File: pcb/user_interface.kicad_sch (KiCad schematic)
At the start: 18 parts, among them Q6 NTR4003N, SW4 GSPTS0018, SW5 GSPTS0018, SW6 GSPTS0018, SW7 GSPTS0018

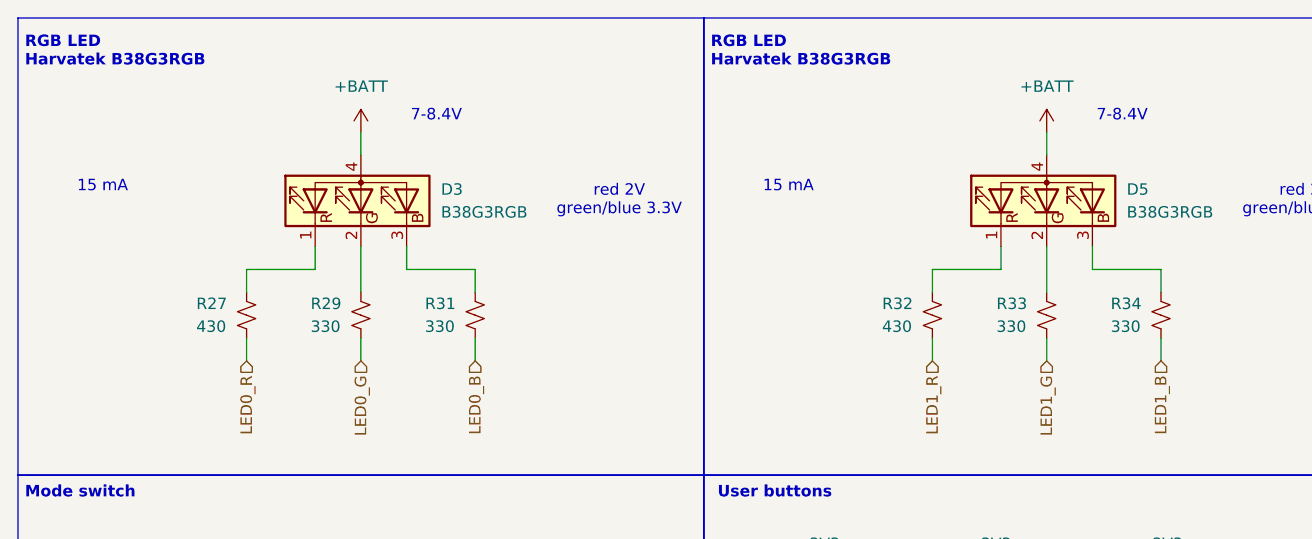
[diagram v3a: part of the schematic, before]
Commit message: Decrease LED current from 15 mA to 10 mA per color
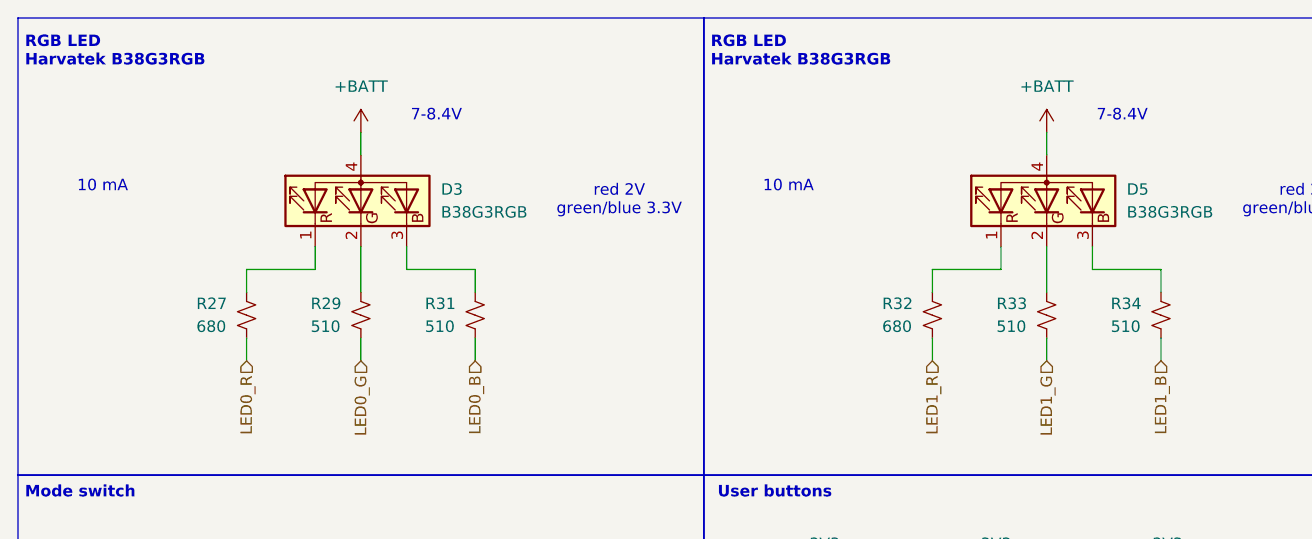
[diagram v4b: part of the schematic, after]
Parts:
- R27, R32: value 430 -> 680
- R29, R31, R33, R34: value 330 -> 510
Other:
- note added: "10 mA"
- note removed: "15 mA"
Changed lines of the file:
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@@
 		)
 	)
-	(text "15 mA"
+	(text "10 mA"
 		(exclude_from_sim no)
 		(at 22.098 31.496 0)
@@
 		)
 	)
-	(text "15 mA"
+	(text "10 mA"
 		(exclude_from_sim no)
 		(at 98.298 31.496 0)
@@
 			)
 		)
-		(property "Value" "330"
+		(property "Value" "510"
 			(at 45.212 46.99 0)
 			(effects
@@
 			)
 		)
-		(property "Value" "330"
+		(property "Value" "510"
 			(at 121.412 46.99 0)
 			(effects
@@
 			)
 		)
-		(property "Value" "430"
+		(property "Value" "680"
 			(at 108.712 46.99 0)
 			(effects
@@
 			)
 		)
-		(property "Value" "330"
+		(property "Value" "510"
 			(at 134.112 46.99 0)
 			(effects
@@
 			)
 		)
-		(property "Value" "430"
+		(property "Value" "680"
 			(at 32.512 46.99 0)
 			(effects
@@
 			)
 		)
-		(property "Value" "330"
+		(property "Value" "510"
 			(at 57.912 46.99 0)
 			(effects

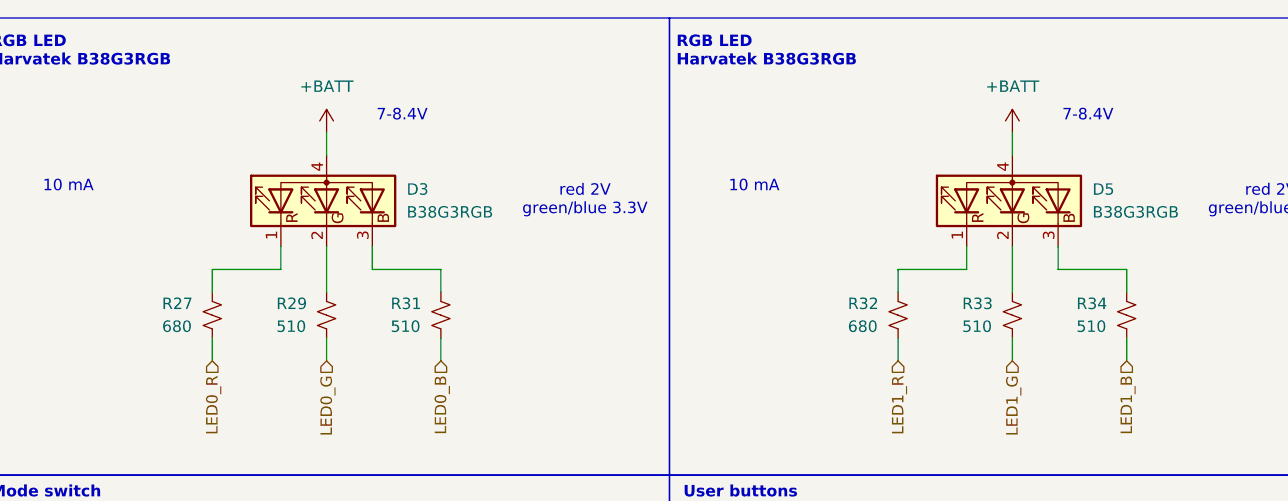
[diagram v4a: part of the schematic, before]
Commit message: Finish routing with rotated STM32
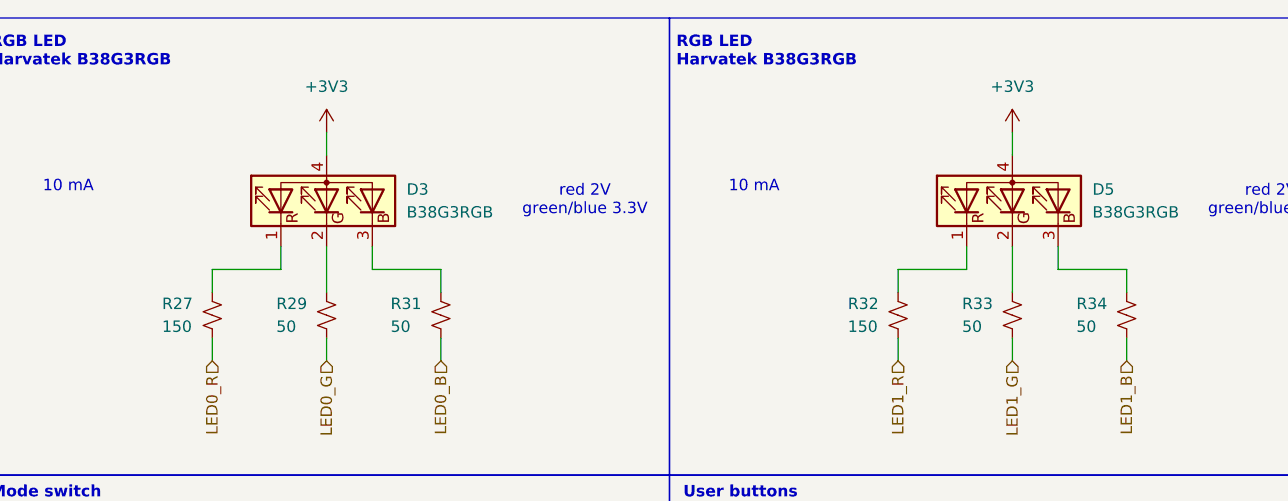
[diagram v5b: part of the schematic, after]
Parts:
- R27, R32: value 680 -> 150
- R29, R31, R33, R34: value 510 -> 50
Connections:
- net +BATT is gone; now on net +3V3: D3.4 (A), D5.4 (A)
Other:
- note removed: "7-8.4V"
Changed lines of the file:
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@@
-		)
-	)
-	(text "7-8.4V"
-		(exclude_from_sim no)
-		(at 59.182 23.622 0)
-		(effects
-			(font
-				(size 1.27 1.27)
-			)
-		)
-	)
-	(text "7-8.4V"
-		(exclude_from_sim no)
-		(at 135.382 23.622 0)
-		(effects
-			(font
-				(size 1.27 1.27)
-			)
 		)
 	)
@@
 			)
 		)
-		(property "Value" "510"
+		(property "Value" "50"
 			(at 45.212 46.99 0)
 			(effects
@@
 	(symbol
 		(lib_id "power:+3V3")
+		(at 127 25.4 0)
+		(unit 1)
+		(exclude_from_sim no)
+		(in_bom yes)
+		(on_board yes)
+		(dnp no)
+		(fields_autoplaced yes)
+		(property "Reference" "#PWR065"
+			(at 127 29.21 0)
+			(effects
+				(font
+					(size 1.27 1.27)
+				)
+				(hide yes)
+			)
+		)
+		(property "Value" "+3V3"
+			(at 127 20.32 0)
+			(effects
+				(font
+					(size 1.27 1.27)
+				)
+			)
+		)
+		(property "Footprint" ""
+			(at 127 25.4 0)
+			(effects
+				(font
+					(size 1.27 1.27)
+				)
+				(hide yes)
+			)
+		)
+		(property "Datasheet" ""
+			(at 127 25.4 0)
+			(effects
+				(font
+					(size 1.27 1.27)
+				)
+				(hide yes)
+			)
+		)
+		(property "Description" "Power symbol creates a global label with name \"+3V3\""
+			(at 127 25.4 0)
+			(effects
+				(font
+					(size 1.27 1.27)
+				)
+				(hide yes)
+			)
+		)
+		(pin "1"
+		)
+		(instances
+			(project ""
+				(path "/1f4fd4ed-9886-4375-a5ac-dc32d5760936/0a32b07f-7988-40ae-8006-b298a5ae2a50"
+					(reference "#PWR065")
+					(unit 1)
+				)
+			)
+		)
+	)
+	(symbol
+		(lib_id "power:+3V3")
 		(at 120.65 76.2 0)
 		(unit 1)
@@
 			)
 		)
-		(property "Value" "510"
+		(property "Value" "50"
 			(at 121.412 46.99 0)
 			(effects
@@
 			)
 		)
-		(property "Value" "680"
+		(property "Value" "150"
 			(at 108.712 46.99 0)
 			(effects
@@
 			)
 		)
-		(property "Value" "510"
+		(property "Value" "50"
 			(at 134.112 46.99 0)
 			(effects
@@
 				(path "/1f4fd4ed-9886-4375-a5ac-dc32d5760936/0a32b07f-7988-40ae-8006-b298a5ae2a50"
 					(reference "R34")
+					(unit 1)
+				)
+			)
+		)
+	)
+	(symbol
+		(lib_id "power:+3V3")
+		(at 50.8 25.4 0)
+		(unit 1)
+		(exclude_from_sim no)
+		(in_bom yes)
+		(on_board yes)
+		(dnp no)
+		(fields_autoplaced yes)
+		(property "Reference" "#PWR059"
+			(at 50.8 29.21 0)
+			(effects
+				(font
+					(size 1.27 1.27)
+				)
+				(hide yes)
+			)
+		)
+		(property "Value" "+3V3"
+			(at 50.8 20.32 0)
+			(effects
+				(font
+					(size 1.27 1.27)
+				)
+			)
+		)
+		(property "Footprint" ""
+			(at 50.8 25.4 0)
+			(effects
+				(font
+					(size 1.27 1.27)
+				)
+				(hide yes)
+			)
+		)
+		(property "Datasheet" ""
+			(at 50.8 25.4 0)
+			(effects
+				(font
+					(size 1.27 1.27)
+				)
+				(hide yes)
+			)
+		)
+		(property "Description" "Power symbol creates a global label with name \"+3V3\""
+			(at 50.8 25.4 0)
+			(effects
+				(font
+					(size 1.27 1.27)
+				)
+				(hide yes)
+			)
+		)
+		(pin "1"
+		)
+		(instances
+			(project ""
+				(path "/1f4fd4ed-9886-4375-a5ac-dc32d5760936/0a32b07f-7988-40ae-8006-b298a5ae2a50"
+					(reference "#PWR059")
 					(unit 1)
 				)
@@
 	)
 	(symbol
-		(lib_id "power:+BATT")
-		(at 50.8 25.4 0)
-		(unit 1)
-		(exclude_from_sim no)
-		(in_bom yes)
-		(on_board yes)
-		(dnp no)
-		(fields_autoplaced yes)
-		(property "Reference" "#PWR059"
-			(at 50.8 29.21 0)
-			(effects
-				(font
-					(size 1.27 1.27)
-				)
-				(hide yes)
-			)
-		)
-		(property "Value" "+BATT"
-			(at 50.8 20.32 0)
-			(effects
-				(font
-					(size 1.27 1.27)
-				)
-			)
-		)
-		(property "Footprint" ""
-			(at 50.8 25.4 0)
-			(effects
-				(font
-					(size 1.27 1.27)
-				)
-				(hide yes)
-			)
-		)
-		(property "Datasheet" ""
-			(at 50.8 25.4 0)
-			(effects
-				(font
-					(size 1.27 1.27)
-				)
-				(hide yes)
-			)
-		)
-		(property "Description" "Power symbol creates a global label with name \"+BATT\""
-			(at 50.8 25.4 0)
-			(effects
-				(font
-					(size 1.27 1.27)
-				)
-				(hide yes)
-			)
-		)
-		(pin "1"
-		)
-		(instances
-			(project "airbrake_mod"
-				(path "/1f4fd4ed-9886-4375-a5ac-dc32d5760936/0a32b07f-7988-40ae-8006-b298a5ae2a50"
-					(reference "#PWR059")
-					(unit 1)
-				)
-			)
-		)
-	)
-	(symbol
 		(lib_id "Transistor_FET:Q_NMOS_GSD")
 		(at 60.96 152.4 0)
@@
 	)
 	(symbol
-		(lib_id "power:+BATT")
-		(at 127 25.4 0)
-		(unit 1)
-		(exclude_from_sim no)
-		(in_bom yes)
-		(on_board yes)
-		(dnp no)
-		(fields_autoplaced yes)
-		(property "Reference" "#PWR065"
-			(at 127 29.21 0)
-			(effects
-				(font
-					(size 1.27 1.27)
-				)
-				(hide yes)
-			)
-		)
-		(property "Value" "+BATT"
-			(at 127 20.32 0)
-			(effects
-				(font
-					(size 1.27 1.27)
-				)
-			)
-		)
-		(property "Footprint" ""
-			(at 127 25.4 0)
-			(effects
-				(font
-					(size 1.27 1.27)
-				)
-				(hide yes)
-			)
-		)
-		(property "Datasheet" ""
-			(at 127 25.4 0)
-			(effects
-				(font
-					(size 1.27 1.27)
-				)
-				(hide yes)
-			)
-		)
-		(property "Description" "Power symbol creates a global label with name \"+BATT\""
-			(at 127 25.4 0)
-			(effects
-				(font
-					(size 1.27 1.27)
-				)
-				(hide yes)
-			)
-		)
-		(pin "1"
-		)
-		(instances
-			(project "airbrake_mod"
-				(path "/1f4fd4ed-9886-4375-a5ac-dc32d5760936/0a32b07f-7988-40ae-8006-b298a5ae2a50"
-					(reference "#PWR065")
-					(unit 1)
-				)
-			)
-		)
-	)
-	(symbol
 		(lib_id "Device:R_Small_US")
 		(at 38.1 45.72 0)
@@
 			)
 		)
-		(property "Value" "680"
+		(property "Value" "150"
 			(at 32.512 46.99 0)
 			(effects
@@
 			)
 		)
-		(property "Value" "510"
+		(property "Value" "50"
 			(at 57.912 46.99 0)
 			(effects

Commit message: Add buck enable switch
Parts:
- S1: footprint SW_SameSky_RDS4-8S-1012-73-RA-254-D-67:SW_RDS4-8S-1012-73-RA-254-D-67 -> SW_SameSky:SW_SameSky_RDS4-8S-1012-73-RA-254-D-67
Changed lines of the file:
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@@
 		(dnp no)
 		(fields_autoplaced yes)
-		(property "Reference" "#PWR071"
+		(property "Reference" "#PWR072"
 			(at 158.75 80.01 0)
 			(effects
@@
 			(project "airbrake_mod"
 				(path "/1f4fd4ed-9886-4375-a5ac-dc32d5760936/0a32b07f-7988-40ae-8006-b298a5ae2a50"
-					(reference "#PWR071")
+					(reference "#PWR072")
 					(unit 1)
 				)
@@
 		(dnp no)
 		(fields_autoplaced yes)
-		(property "Reference" "#PWR066"
+		(property "Reference" "#PWR067"
 			(at 63.5 171.45 0)
 			(effects
@@
 			(project "airbrake_mod"
 				(path "/1f4fd4ed-9886-4375-a5ac-dc32d5760936/0a32b07f-7988-40ae-8006-b298a5ae2a50"
-					(reference "#PWR066")
+					(reference "#PWR067")
 					(unit 1)
 				)
@@
 		(dnp no)
 		(fields_autoplaced yes)
-		(property "Reference" "#PWR065"
+		(property "Reference" "#PWR066"
 			(at 63.5 130.81 0)
 			(effects
@@
 			(project ""
 				(path "/1f4fd4ed-9886-4375-a5ac-dc32d5760936/0a32b07f-7988-40ae-8006-b298a5ae2a50"
-					(reference "#PWR065")
+					(reference "#PWR066")
 					(unit 1)
 				)
@@
 		(dnp no)
 		(fields_autoplaced yes)
-		(property "Reference" "#PWR064"
+		(property "Reference" "#PWR065"
 			(at 50.8 171.45 0)
 			(effects
@@
 			(project "airbrake_mod"
 				(path "/1f4fd4ed-9886-4375-a5ac-dc32d5760936/0a32b07f-7988-40ae-8006-b298a5ae2a50"
-					(reference "#PWR064")
+					(reference "#PWR065")
 					(unit 1)
 				)
@@
 		(dnp no)
 		(fields_autoplaced yes)
-		(property "Reference" "#PWR069"
+		(property "Reference" "#PWR070"
 			(at 127 29.21 0)
 			(effects
@@
 			(project ""
 				(path "/1f4fd4ed-9886-4375-a5ac-dc32d5760936/0a32b07f-7988-40ae-8006-b298a5ae2a50"
-					(reference "#PWR069")
+					(reference "#PWR070")
 					(unit 1)
 				)
@@
 		(dnp no)
 		(fields_autoplaced yes)
-		(property "Reference" "#PWR068"
+		(property "Reference" "#PWR069"
 			(at 120.65 80.01 0)
 			(effects
@@
 			(project "airbrake_mod"
 				(path "/1f4fd4ed-9886-4375-a5ac-dc32d5760936/0a32b07f-7988-40ae-8006-b298a5ae2a50"
-					(reference "#PWR068")
+					(reference "#PWR069")
 					(unit 1)
 				)
@@
 		(dnp no)
 		(fields_autoplaced yes)
-		(property "Reference" "#PWR070"
+		(property "Reference" "#PWR071"
 			(at 139.7 80.01 0)
 			(effects
@@
 			(project "airbrake_mod"
 				(path "/1f4fd4ed-9886-4375-a5ac-dc32d5760936/0a32b07f-7988-40ae-8006-b298a5ae2a50"
-					(reference "#PWR070")
+					(reference "#PWR071")
 					(unit 1)
 				)
@@
 		(dnp no)
 		(fields_autoplaced yes)
-		(property "Reference" "#PWR063"
+		(property "Reference" "#PWR064"
 			(at 50.8 29.21 0)
 			(effects
@@
 			(project ""
 				(path "/1f4fd4ed-9886-4375-a5ac-dc32d5760936/0a32b07f-7988-40ae-8006-b298a5ae2a50"
-					(reference "#PWR063")
+					(reference "#PWR064")
 					(unit 1)
 				)
@@
 			)
 		)
-		(property "Footprint" "SW_SameSky_RDS4-8S-1012-73-RA-254-D-67:SW_RDS4-8S-1012-73-RA-254-D-67"
+		(property "Footprint" "SW_SameSky:SW_SameSky_RDS4-8S-1012-73-RA-254-D-67"
 			(at 50.8 80.01 0)
 			(effects
@@
 		(dnp no)
 		(fields_autoplaced yes)
-		(property "Reference" "#PWR067"
+		(property "Reference" "#PWR068"
 			(at 101.6 80.01 0)
 			(effects
@@
 			(project ""
 				(path "/1f4fd4ed-9886-4375-a5ac-dc32d5760936/0a32b07f-7988-40ae-8006-b298a5ae2a50"
-					(reference "#PWR067")
-					(unit 1)
-				)
+					(reference "#PWR068")
+					(unit 1)
+				)

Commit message: Add CUR schematic sheet title block
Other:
- company: (none) -> Clarkson University Rocketry Team
- title: (none) -> Air Brakes Module
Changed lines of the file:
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@@
 	(generator_version "9.0")
 	(paper "A4")
+	(title_block
+		(title "Air Brakes Module")
+		(date "2025-11-23")
+		(company "Clarkson University Rocketry Team")
+	)
 	(rectangle
 		(start 88.9 63.5)
